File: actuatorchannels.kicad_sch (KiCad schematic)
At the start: 120 parts, among them J10 ACT CH9, J11 ACT CH10, J12 ACT CH11, J13 ACT CH12, J14 ACT CH13, J15 ACT CH14, J16 ACT CH15, J17 ACT CH16, J2 ACT CH1, J3 ACT CH2, J4 ACT CH3, J5 ACT CH4, J6 ACT CH5, J7 ACT CH6, J8 ACT CH7, J9 ACT CH8, U10 TLP241A, U11 TLP241A, U12 TLP241A, U13 TLP241A, U14 TLP241A, U15 TLP241A, U16 TLP241A, U17 TLP241A, U18 TLP241A, U19 PCA9534, U20 PCA9534, U3 TLP241A, U4 TLP241A, U5 TLP241A, U6 TLP241A, U7 TLP241A, U8 TLP241A, U9 TLP241A

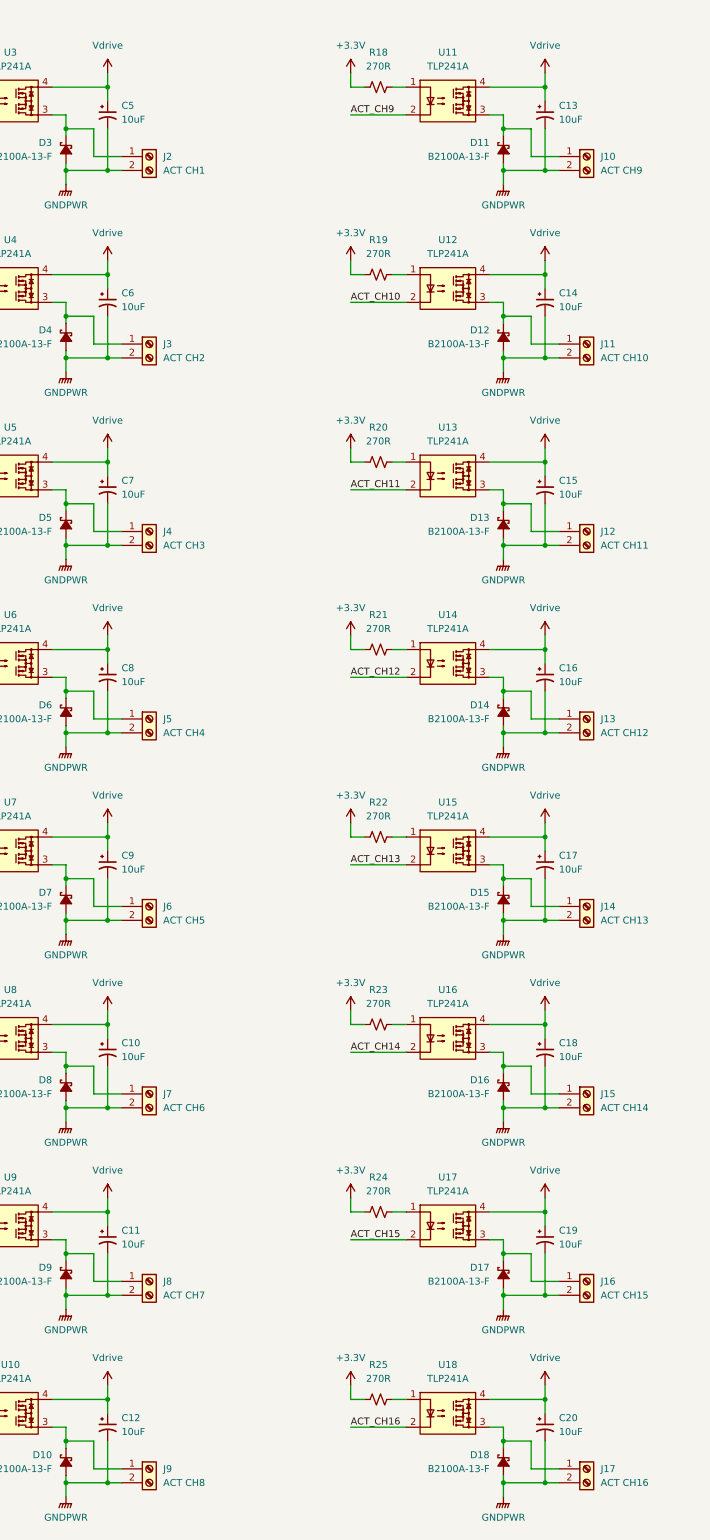
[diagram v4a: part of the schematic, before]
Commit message: 130x130 and arranged feedback
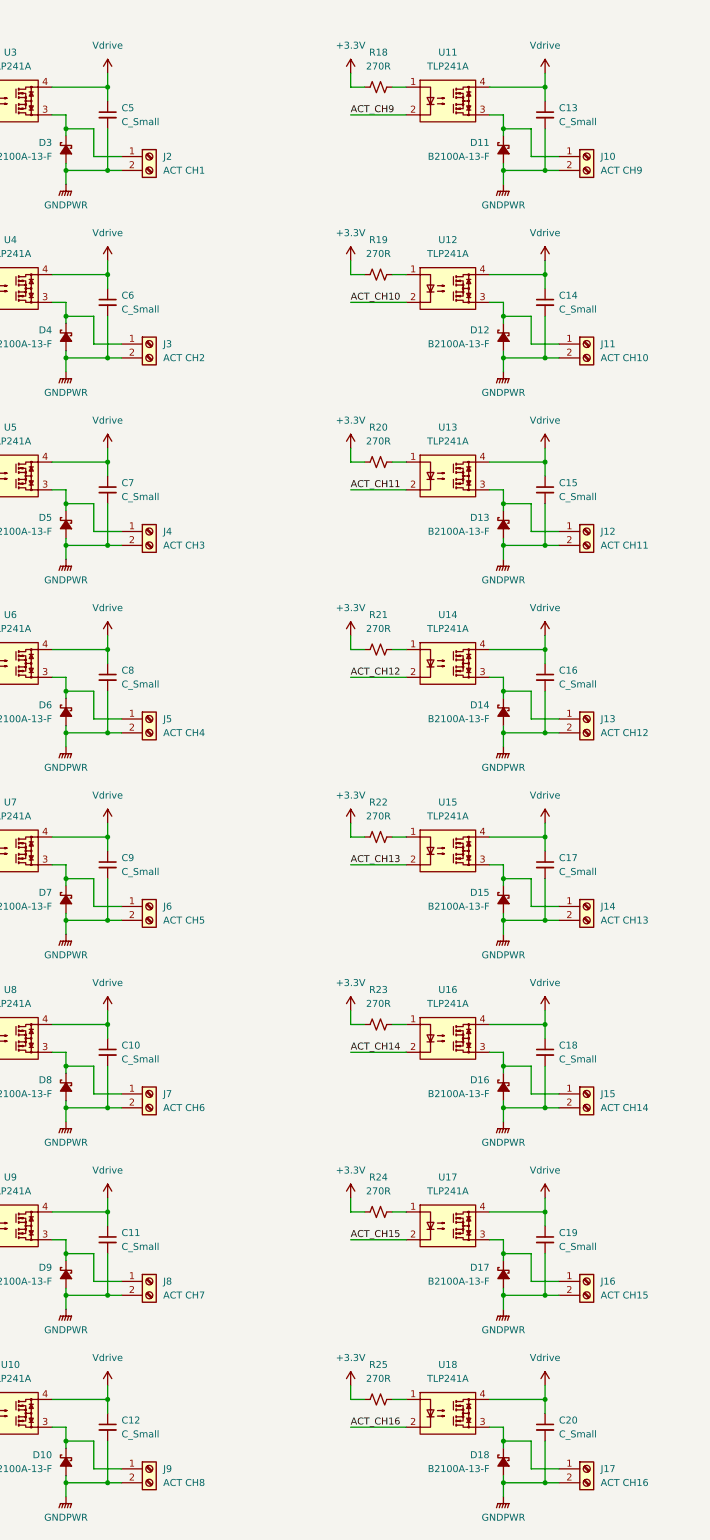
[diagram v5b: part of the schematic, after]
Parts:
- removed C10, C11, C12, C13, C14, C15, C16, C17, C18, C19, C20, C5, C6, C7, C8, C9: 10uF, Capacitor_SMD:CP_Elec_4x5.8, symbol Device:C_Polarized_Small_US
- added C10, C11, C12, C13, C14, C15, C16, C17, C18, C19, C20, C5, C6, C7, C8, C9: C_Small, Capacitor_SMD:C_1210_3225Metric, symbol Device:C_Small
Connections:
- net GNDPWR: now also C10.2, C11.2, C12.2, C13.2, C14.2, C15.2, C16.2, C17.2, C18.2, C19.2, C20.2, C5.2, C6.2, C7.2, C8.2, C9.2
- net Vdrive: now also C10.1, C11.1, C12.1, C13.1, C14.1, C15.1, C16.1, C17.1, C18.1, C19.1, C20.1, C5.1, C6.1, C7.1, C8.1, C9.1

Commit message: Gerbers and passive value update
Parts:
- C10, C11, C12, C13, C14, C15, C16, C17, C18, C19, C20, C5, C6, C7, C8, C9: value C_Small -> 10uF

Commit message: Finishing up part selection
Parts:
- C21, C22: MPN (none) -> GRT188R61H105KE13D
- C23, C24: MPN (none) -> GRM188R72A104KA35D
- R26, R27, R28, R29, R30, R31, R32, R33, R34, R35, R36, R37, R38, R39, R40, R41: MPN (none) -> RC0603FR-07470RL
